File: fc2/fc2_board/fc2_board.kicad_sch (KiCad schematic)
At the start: 12 parts, among them U1 MPU-6050, U2 STM32G070RBTx, U3 SAM-M10Q-00B

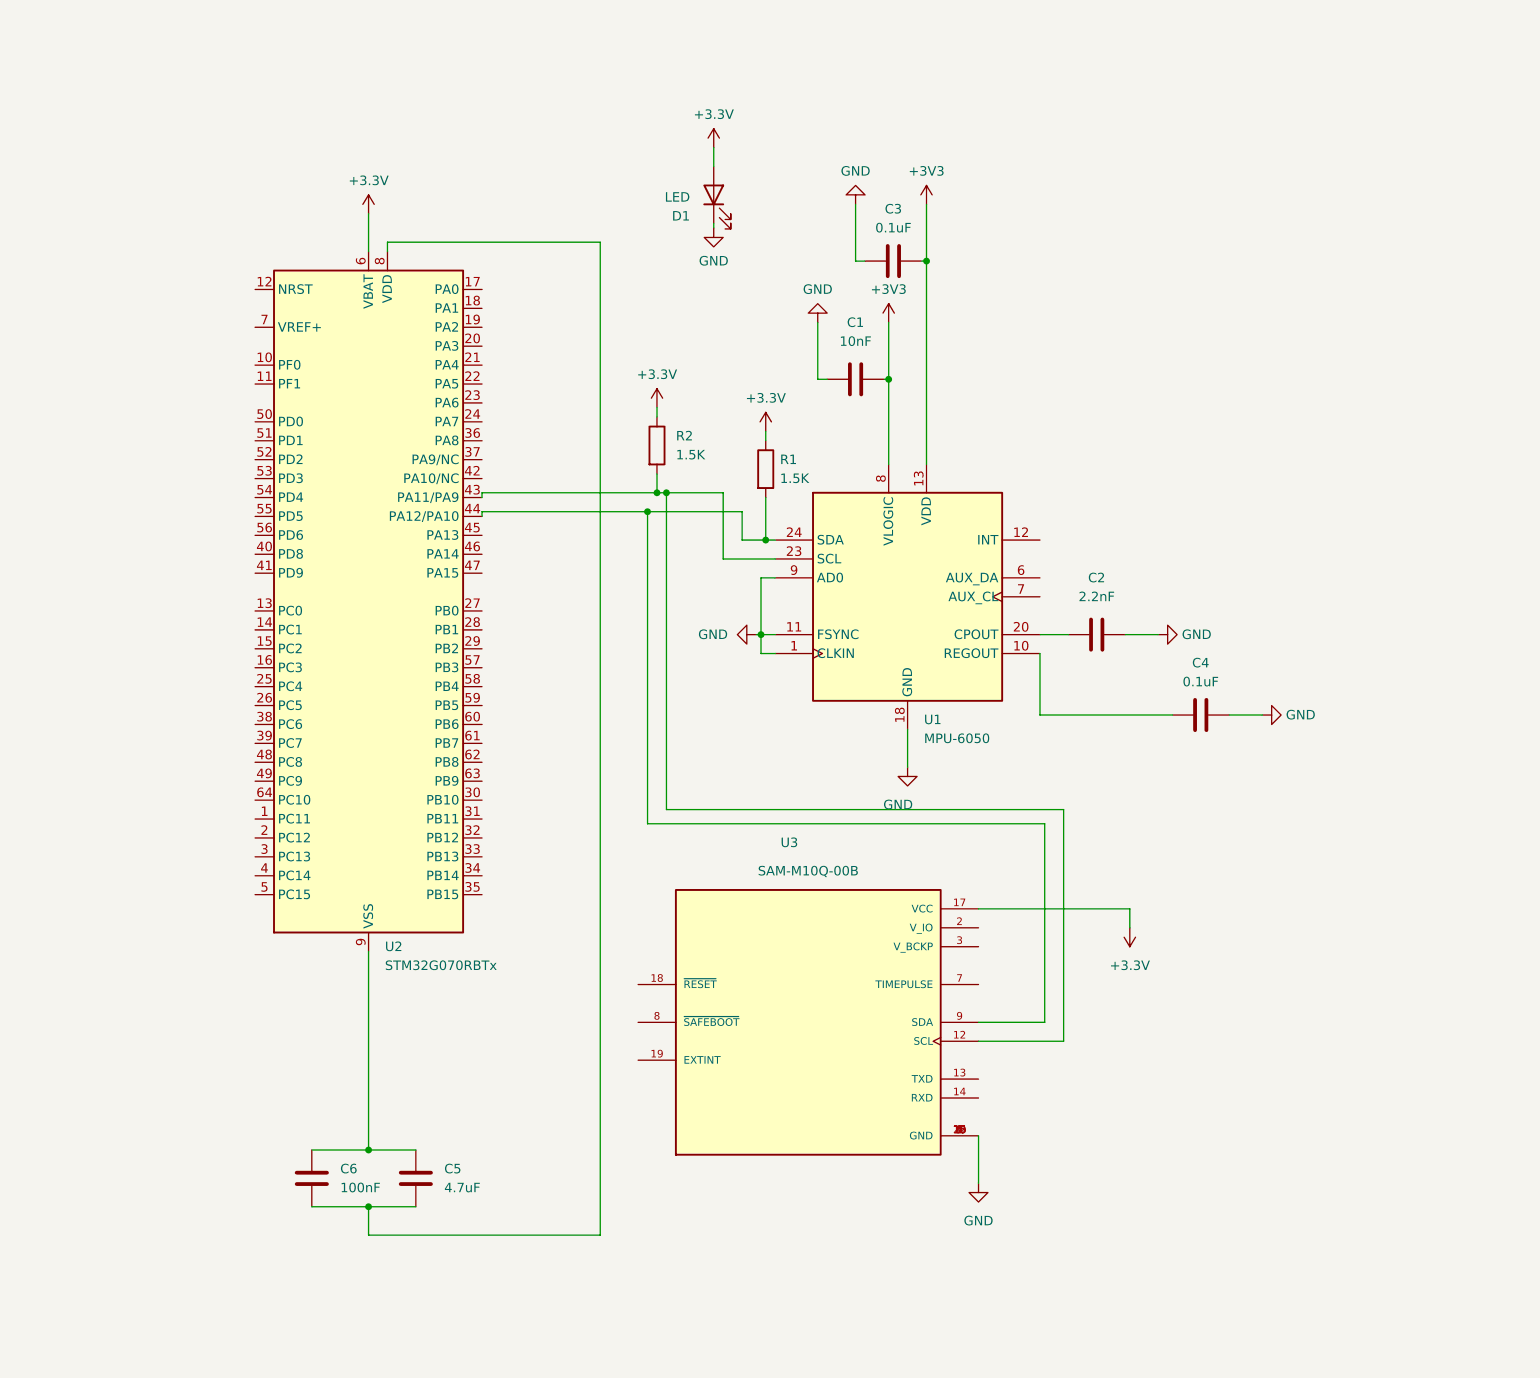
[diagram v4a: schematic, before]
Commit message: kicad: add esc integration
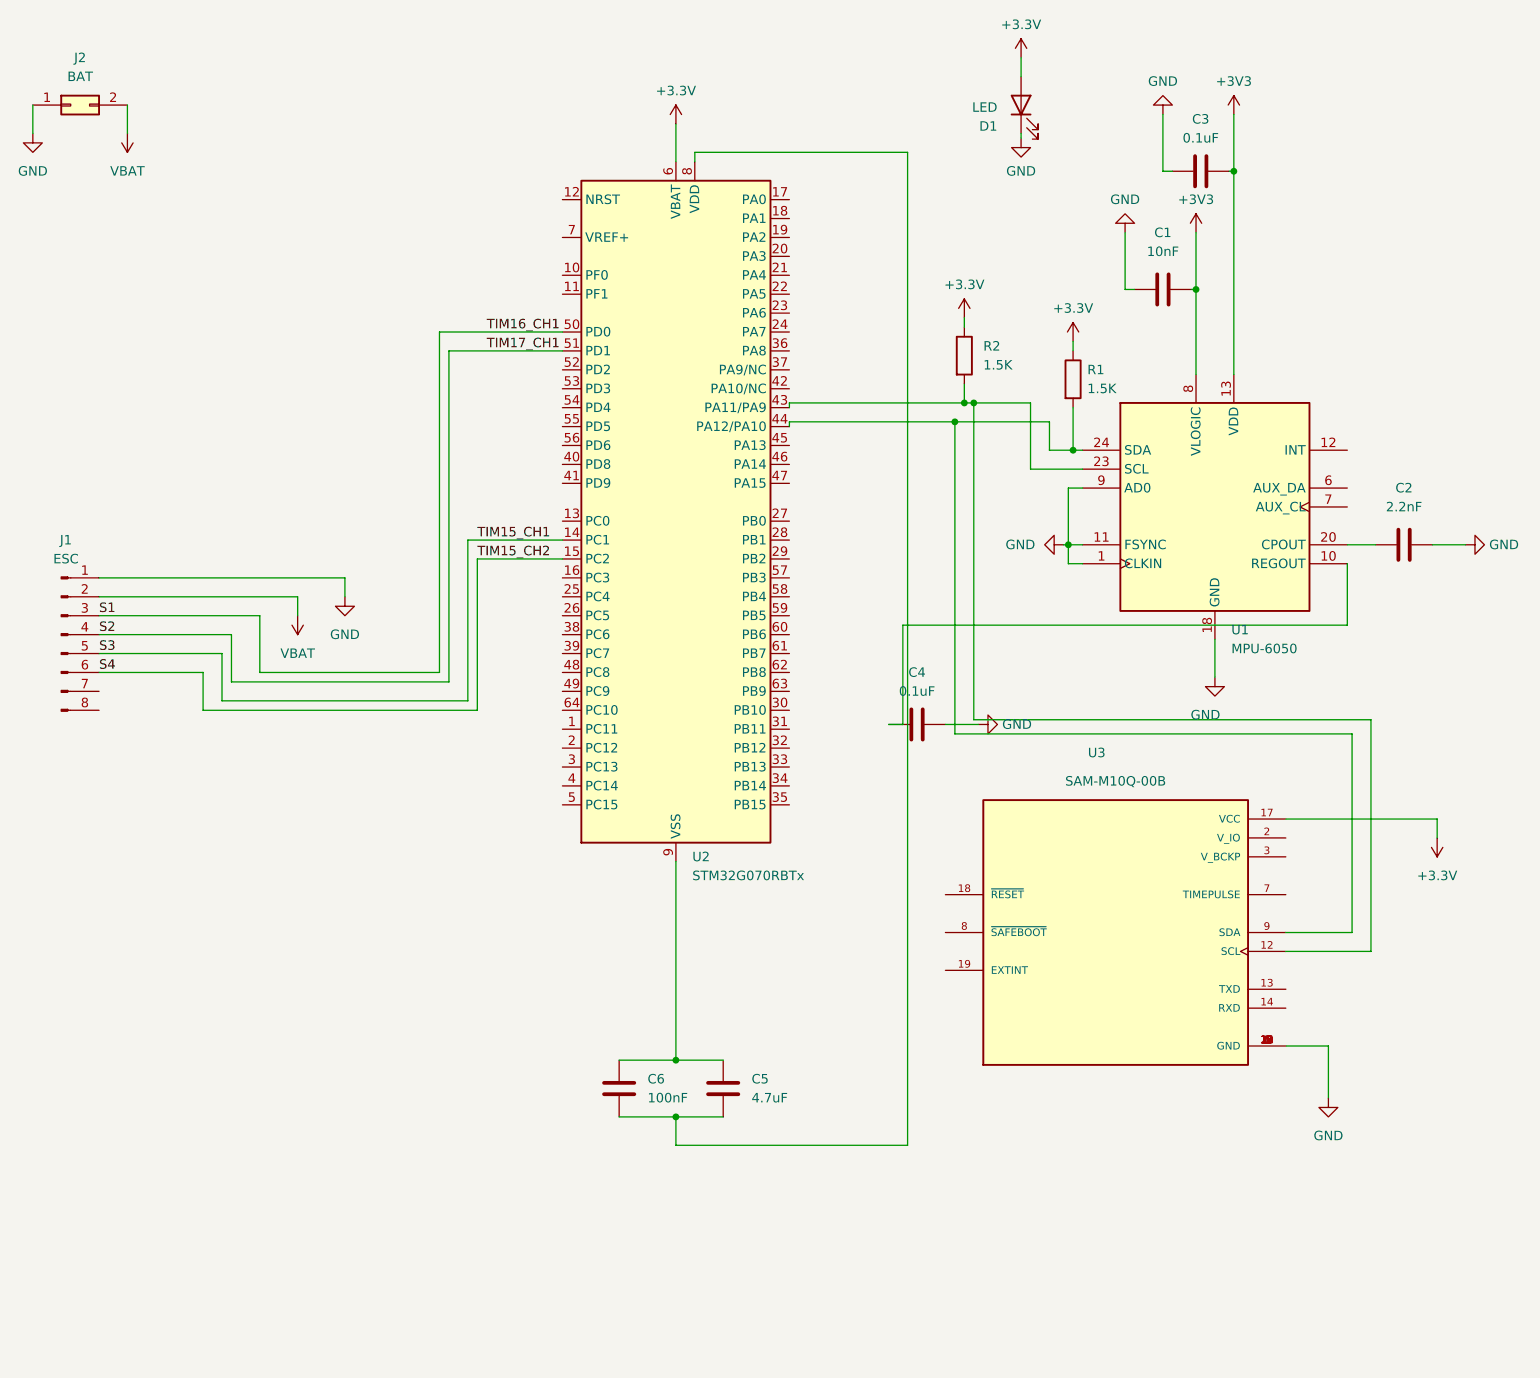
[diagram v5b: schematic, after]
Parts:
- added J1: ESC, Connector_JST, symbol Connector:Conn_01x08_Pin
- added J2: BAT, symbol Connector_Generic:Conn_02x01
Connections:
- net GND: now also J1.1 (Pin_1), J2.1 (Pin_1)
- net S3: now reaches U2.14 (PC1)
- net S3: now also J1.5 (Pin_5)
- net S4: now reaches U2.15 (PC2)
- net S4: now also J1.6 (Pin_6)
- net S1: now reaches U2.50 (PD0)
- net S1: now also J1.3 (Pin_3)
- net S2: now reaches U2.51 (PD1)
- net S2: now also J1.4 (Pin_4)
- new net VBAT: J1.2 (Pin_2), J2.2 (Pin_2)
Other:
- moved on the sheet: C1, C2, C3, C4, C5, C6, D1, R1, R2, U1, U2, U3

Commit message: kicad: add BME280
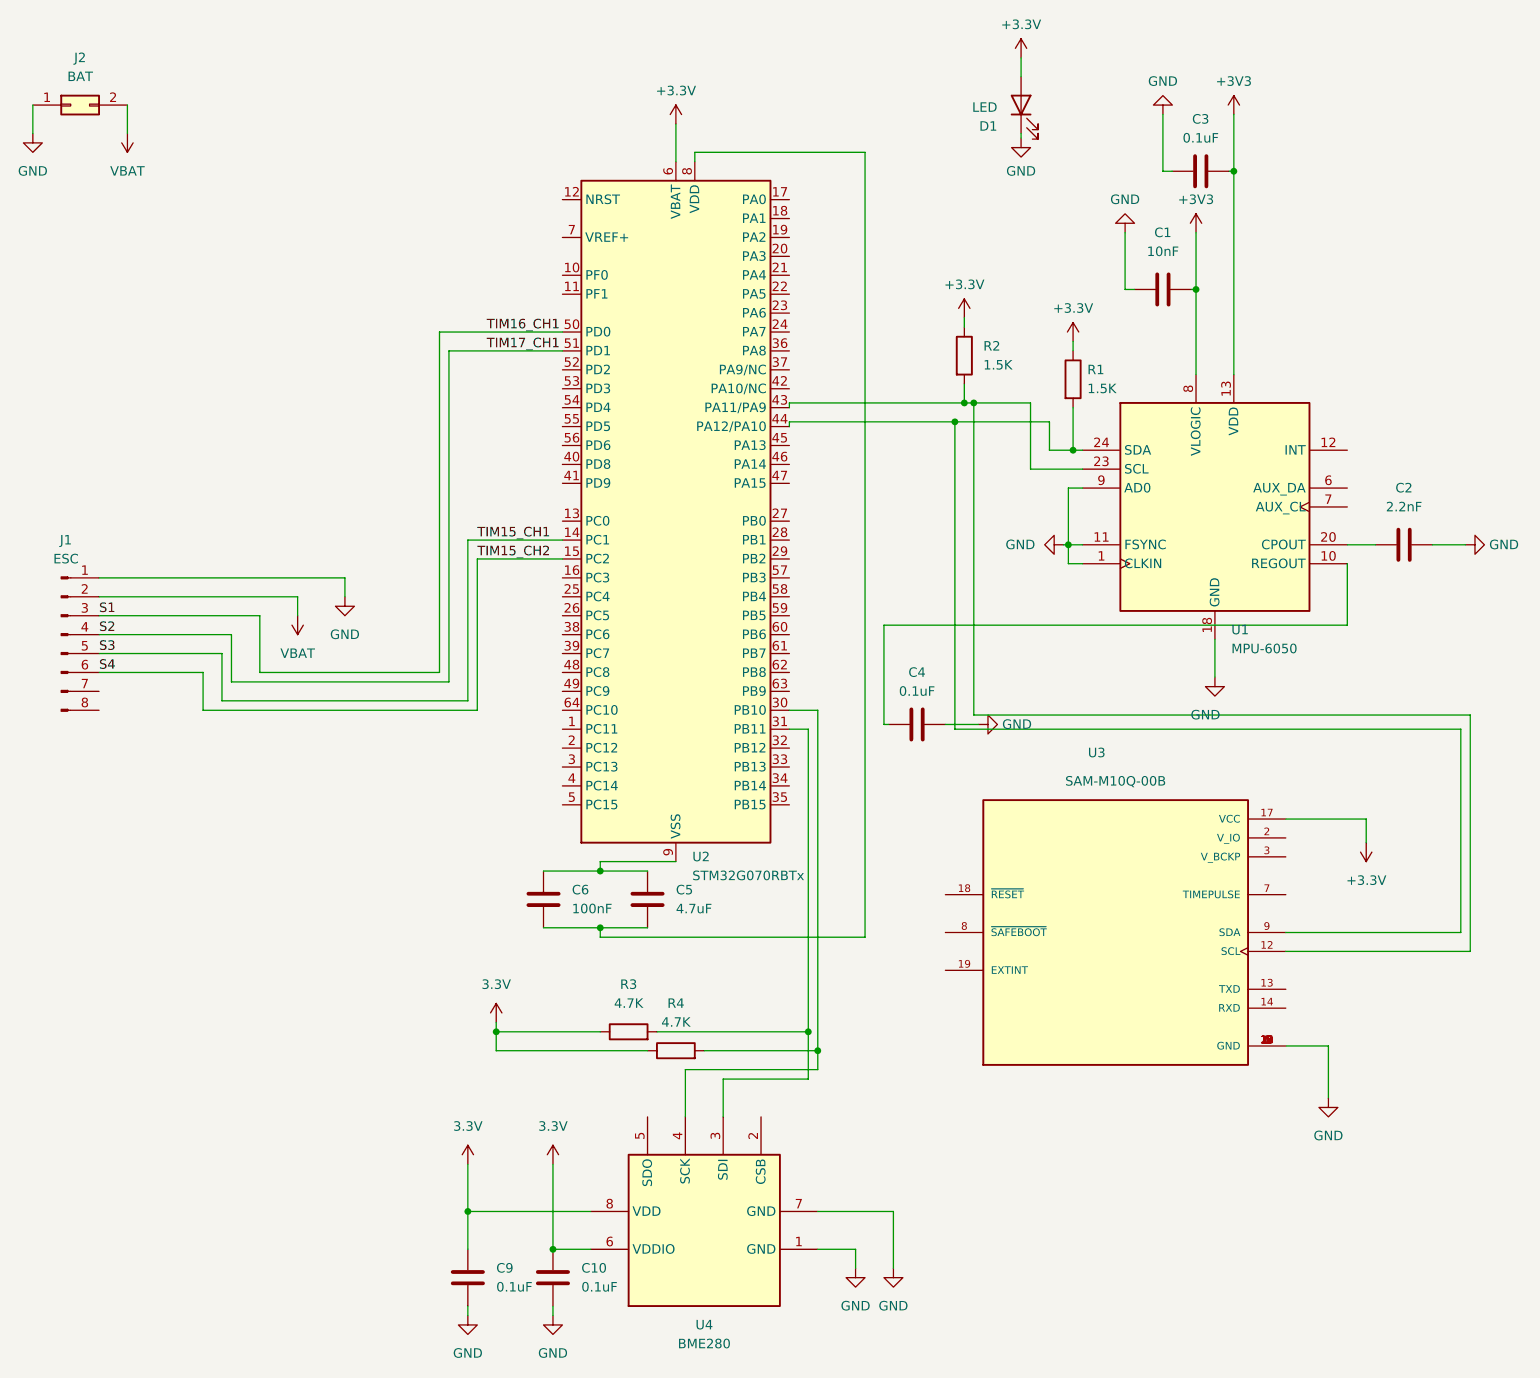
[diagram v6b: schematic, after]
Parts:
- added C10, C9: 0.1uF, symbol Device:C
- added R3, R4: 4.7K, symbol Device:R
- added U4: BME280, Package_LGA:Bosch_LGA-8_2.5x2.5mm_P0.65mm_ClockwisePinNumbering, symbol Sensor:BME280
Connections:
- net GND: now also C10.2, C9.2, U4.1 (GND), U4.7 (GND)
- net at U2.30 (PB10): now also R4.2, U4.4 (SCK)
- net at U2.31 (PB11): now also R3.2, U4.3 (SDI)
- new net 3.3V: C10.1, C9.1, R3.1, R4.1, U4.6 (VDDIO), U4.8 (VDD)
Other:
- moved on the sheet: C5, C6

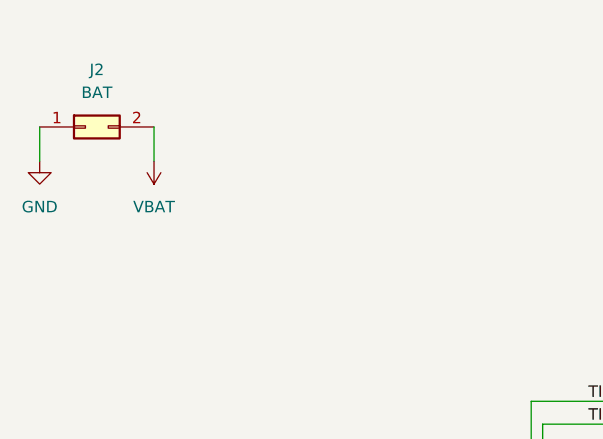
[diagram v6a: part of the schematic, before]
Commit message: kicad: add label to batt
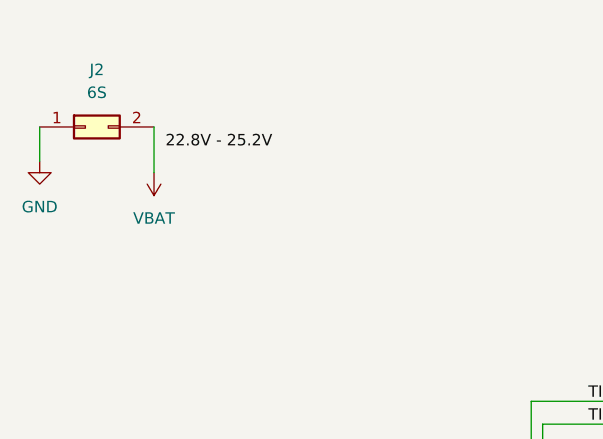
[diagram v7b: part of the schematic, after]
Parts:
- J2: value BAT -> 6S
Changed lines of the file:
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@@
 	(wire
 		(pts
-			(xy 193.675 36.83) (xy 193.675 29.21)
+			(xy 54.61 27.94) (xy 54.61 33.02)
 		)
 		(stroke
@@
 	(wire
 		(pts
-			(xy 125.73 152.4) (xy 146.05 152.4)
+			(xy 193.675 36.83) (xy 193.675 29.21)
 		)
 		(stroke
@@
 	(wire
 		(pts
-			(xy 180.975 86.995) (xy 182.88 86.995)
+			(xy 125.73 152.4) (xy 146.05 152.4)
 		)
 		(stroke
@@
 	(wire
 		(pts
-			(xy 118.11 129.54) (xy 128.27 129.54)
+			(xy 180.975 86.995) (xy 182.88 86.995)
 		)
 		(stroke
@@
 	(wire
 		(pts
-			(xy 233.68 111.76) (xy 233.68 139.065)
+			(xy 118.11 129.54) (xy 128.27 129.54)
 		)
 		(stroke
@@
 	(wire
 		(pts
-			(xy 54.61 27.94) (xy 54.61 31.75)
+			(xy 233.68 111.76) (xy 233.68 139.065)
 		)
 		(stroke
@@
 		)
 	)
+	(label "22.8V - 25.2V"
+		(at 55.88 30.48 0)
+		(fields_autoplaced yes)
+		(effects
+			(font
+				(size 1.27 1.27)
+			)
+			(justify left bottom)
+		)
+	)
 	(label "S2"
 		(at 50.8 99.06 0)
@@
 			)
 		)
-		(property "Value" "BAT"
+		(property "Value" "6S"
 			(at 48.26 24.13 0)
 			(effects
@@
 	(symbol
 		(lib_id "power:VCC")
-		(at 54.61 31.75 180)
+		(at 54.61 33.02 180)
 		(unit 1)
 		(exclude_from_sim no)
@@
 		(fields_autoplaced yes)
 		(property "Reference" "#PWR019"
-			(at 54.61 27.94 0)
+			(at 54.61 29.21 0)
 			(effects
 				(font
@@
 		)
 		(property "Value" "VBAT"
-			(at 54.61 36.83 0)
+			(at 54.61 38.1 0)
 			(effects
 				(font
@@
 		)
 		(property "Footprint" ""
-			(at 54.61 31.75 0)
+			(at 54.61 33.02 0)
 			(effects
 				(font
@@
 		)
 		(property "Datasheet" ""
-			(at 54.61 31.75 0)
+			(at 54.61 33.02 0)
 			(effects
 				(font
@@
 		)
 		(property "Description" "Power symbol creates a global label with name \"VCC\""
-			(at 54.61 31.75 0)
+			(at 54.61 33.02 0)
 			(effects
 				(font
